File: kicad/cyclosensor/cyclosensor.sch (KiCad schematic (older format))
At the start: 5 parts, among them J1 RJ14, J2 RJ14, U1 TCRT5000, U2 TCRT5000

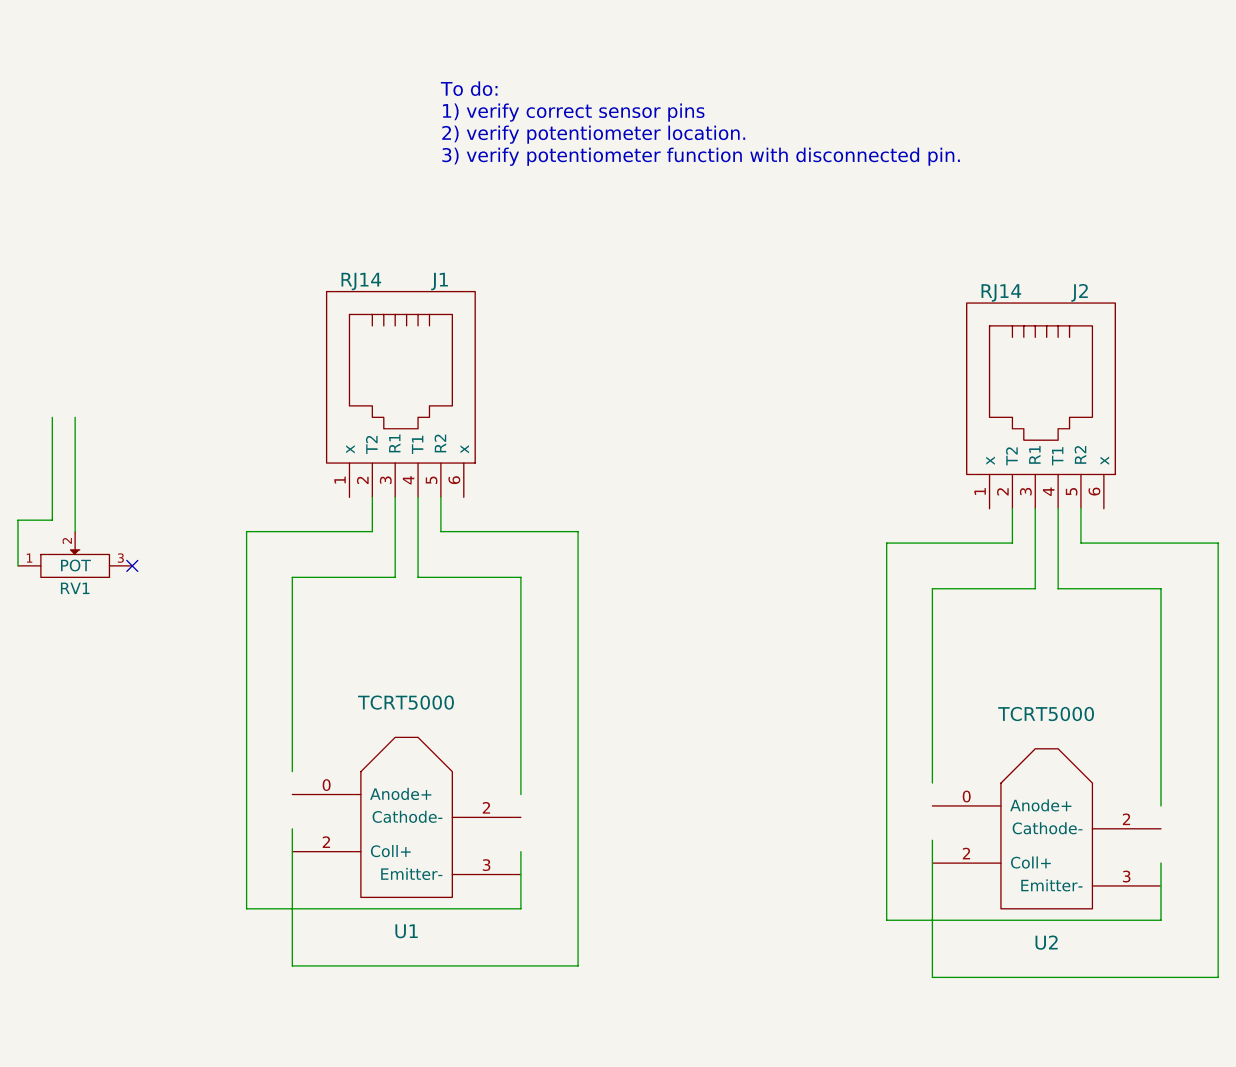
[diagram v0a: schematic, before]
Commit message: updating basic cyclo-sensor.  Still need to verify with actual cyclophone.
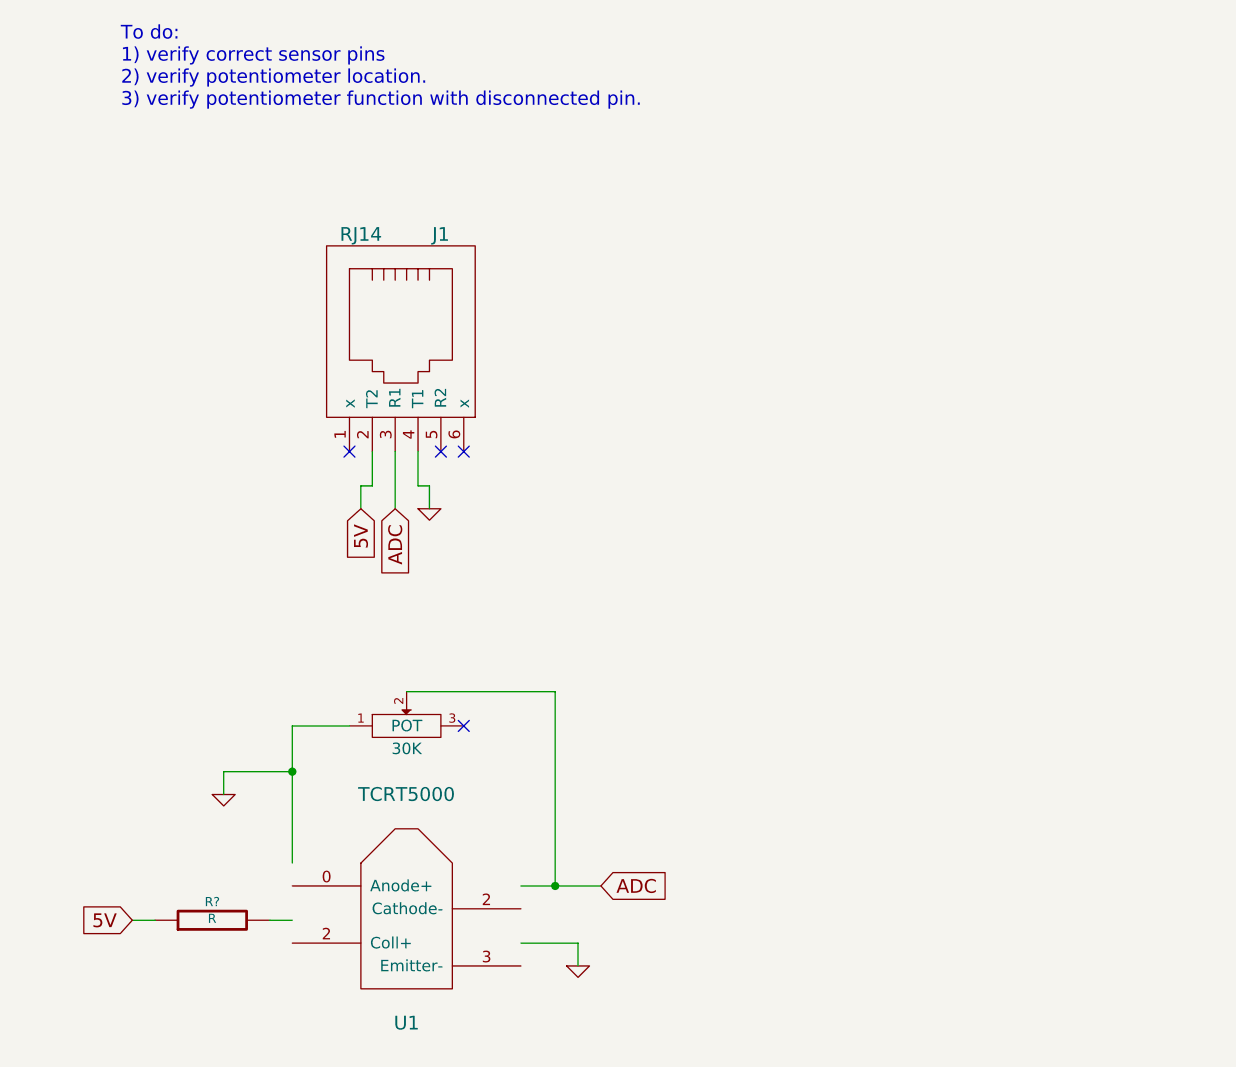
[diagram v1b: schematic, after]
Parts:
- removed J2: RJ14, ~, symbol RJ14
- removed RV1: POT, symbol POT
- removed U2: TCRT5000, symbol TCRT5000
- added 30K: POT, ~, symbol POT
- added R?: R, ~, symbol R
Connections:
- net labels added: 5V, ADC, GND
- wire segments 36 -> 20
- no-connect marks 1 -> 4
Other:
- moved on the sheet: J1, U1
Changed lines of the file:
@@
 Sheet 1 1
 Title ""
-Date "2 apr 2014"
+Date "6 apr 2014"
 Rev ""
 Comp ""
@@
 L RJ14 J1
 U 1 1 532FB492
-P 4800 3150
-F 0 "J1" H 5000 3650 60  0000 C CNN
-F 1 "RJ14" H 4650 3650 60  0000 C CNN
-F 2 "~" H 4800 3150 60  0000 C CNN
-F 3 "~" H 4800 3150 60  0000 C CNN
-	1    4800 3150
+P 4800 2950
+F 0 "J1" H 5000 3450 60  0000 C CNN
+F 1 "RJ14" H 4650 3450 60  0000 C CNN
+F 2 "~" H 4800 2950 60  0000 C CNN
+F 3 "~" H 4800 2950 60  0000 C CNN
+	1    4800 2950
 	1    0    0    -1
 $EndComp
@@
 L TCRT5000 U1
 U 1 1 532FB498
-P 4850 4950
-F 0 "U1" H 4850 4400 60  0000 C CNN
-F 1 "TCRT5000" H 4850 5400 60  0000 C CNN
-F 2 "" H 4850 4950 60  0000 C CNN
-F 3 "" H 4850 4950 60  0000 C CNN
-	1    4850 4950
+P 4850 5350
+F 0 "U1" H 4850 4800 60  0000 C CNN
+F 1 "TCRT5000" H 4850 5800 60  0000 C CNN
+F 2 "" H 4850 5350 60  0000 C CNN
+F 3 "" H 4850 5350 60  0000 C CNN
+	1    4850 5350
+	1    0    0    -1
+$EndComp
+Text Notes 3600 1900 0    60   ~ 0
+To do:\n1) verify correct sensor pins\n2) verify potentiometer location.\n3) verify potentiometer function with disconnected pin.
+Text GLabel 4650 3650 3    60   Input ~ 0
+5V
+Text GLabel 4800 3650 3    60   Input ~ 0
+ADC
+$Comp
+L GND #PWR?
+U 1 1 534162D0
+P 4950 3650
+F 0 "#PWR?" H 4950 3650 30  0001 C CNN
+F 1 "GND" H 4950 3580 30  0001 C CNN
+F 2 "" H 4950 3650 60  0000 C CNN
+F 3 "" H 4950 3650 60  0000 C CNN
+	1    4950 3650
+	1    0    0    -1
+$EndComp
+Text GLabel 3650 5450 0    60   Input ~ 0
+5V
+Text GLabel 5700 5300 2    60   Input ~ 0
+ADC
+$Comp
+L GND #PWR?
+U 1 1 534163B6
+P 5600 5650
+F 0 "#PWR?" H 5600 5650 30  0001 C CNN
+F 1 "GND" H 5600 5580 30  0001 C CNN
+F 2 "" H 5600 5650 60  0000 C CNN
+F 3 "" H 5600 5650 60  0000 C CNN
+	1    5600 5650
+	1    0    0    -1
+$EndComp
+$Comp
+L R R?
+U 1 1 534163EA
+P 4000 5450
+F 0 "R?" V 4080 5450 40  0000 C CNN
+F 1 "R" V 4007 5451 40  0000 C CNN
+F 2 "~" V 3930 5450 30  0000 C CNN
+F 3 "~" H 4000 5450 30  0000 C CNN
+	1    4000 5450
+	0    -1   -1   0
+$EndComp
+Wire Wire Line
+	4700 3400 4700 3550
+Wire Wire Line
+	4700 3550 4650 3550
+Wire Wire Line
+	4650 3550 4650 3650
+Wire Wire Line
+	4800 3400 4800 3650
+Wire Wire Line
+	4900 3400 4900 3550
+Wire Wire Line
+	4900 3550 4950 3550
+Wire Wire Line
+	4950 3550 4950 3650
+Wire Wire Line
+	5350 5550 5600 5550
+Wire Wire Line
+	5600 5550 5600 5650
+Wire Wire Line
+	4250 5450 4350 5450
+Wire Wire Line
+	3650 5450 3750 5450
+$Comp
+L POT 30K
+U 1 1 5341646B
+P 4850 4600
+F 0 "30K" H 4850 4500 50  0000 C CNN
+F 1 "POT" H 4850 4600 50  0000 C CNN
+F 2 "~" H 4850 4600 60  0000 C CNN
+F 3 "~" H 4850 4600 60  0000 C CNN
+	1    4850 4600
+	1    0    0    -1
+$EndComp
+$Comp
+L GND #PWR?
+U 1 1 53416487
+P 4050 4900
+F 0 "#PWR?" H 4050 4900 30  0001 C CNN
+F 1 "GND" H 4050 4830 30  0001 C CNN
+F 2 "" H 4050 4900 60  0000 C CNN
+F 3 "" H 4050 4900 60  0000 C CNN
+	1    4050 4900
 	1    0    0    -1
 $EndComp
 Wire Wire Line
-	5350 5150 5350 5400
+	4350 4600 4350 4800
 Wire Wire Line
-	5350 5400 4150 5400
+	4350 4800 4350 5200
 Wire Wire Line
-	4150 5400 4150 3750
+	4350 4600 4600 4600
+Connection ~ 4350 4800
 Wire Wire Line
-	4150 3750 4700 3750
+	4850 4450 5500 4450
 Wire Wire Line
-	4700 3750 4700 3600
+	5500 4450 5500 5300
 Wire Wire Line
-	4350 4800 4350 3950
+	5350 5300 5500 5300
 Wire Wire Line
-	3300 3250 3300 3700
+	5500 5300 5700 5300
+Connection ~ 5500 5300
 Wire Wire Line
-	3400 3250 3400 3750
+	4050 4900 4050 4800
 Wire Wire Line
-	5350 3950 5350 4900
-Wire Wire Line
-	4350 5050 4350 5650
-Wire Wire Line
-	4350 5650 5600 5650
-Wire Wire Line
-	5600 5650 5600 3750
-Wire Wire Line
-	5600 3750 5000 3750
-Wire Wire Line
-	5000 3750 5000 3600
-Text Notes 5000 2150 0    60   ~ 0
-To do:\n1) verify correct sensor pins\n2) verify potentiometer location.\n3) verify potentiometer function with disconnected pin.
-$Comp
-L POT RV1
-U 1 1 5330B579
-P 3400 3900
-F 0 "RV1" H 3400 3800 50  0000 C CNN
-F 1 "POT" H 3400 3900 50  0000 C CNN
-F 2 "" H 3400 3900 60  0000 C CNN
-F 3 "" H 3400 3900 60  0000 C CNN
-	1    3400 3900
-	1    0    0    -1
-$EndComp
-NoConn ~ 3650 3900
-Wire Wire Line
-	3300 3700 3150 3700
-Wire Wire Line
-	3150 3700 3150 3900
-$Comp
-L RJ14 J2
-U 1 1 5338F808
-P 7600 3200
-F 0 "J2" H 7800 3700 60  0000 C CNN
-F 1 "RJ14" H 7450 3700 60  0000 C CNN
-F 2 "~" H 7600 3200 60  0000 C CNN
-F 3 "~" H 7600 3200 60  0000 C CNN
-	1    7600 3200
-	1    0    0    -1
-$EndComp
-$Comp
-L TCRT5000 U2
-U 1 1 5338F80E
-P 7650 5000
-F 0 "U2" H 7650 4450 60  0000 C CNN
-F 1 "TCRT5000" H 7650 5450 60  0000 C CNN
-F 2 "" H 7650 5000 60  0000 C CNN
-F 3 "" H 7650 5000 60  0000 C CNN
-	1    7650 5000
-	1    0    0    -1
-$EndComp
-Wire Wire Line
-	8150 5200 8150 5450
-Wire Wire Line
-	8150 5450 6950 5450
-Wire Wire Line
-	6950 5450 6950 3800
-Wire Wire Line
-	6950 3800 7500 3800
-Wire Wire Line
-	7500 3800 7500 3650
-Wire Wire Line
-	7150 4850 7150 4000
-Wire Wire Line
-	8150 4000 8150 4950
-Wire Wire Line
-	7150 5100 7150 5700
-Wire Wire Line
-	7150 5700 8400 5700
-Wire Wire Line
-	8400 5700 8400 3800
-Wire Wire Line
-	8400 3800 7800 3800
-Wire Wire Line
-	7800 3800 7800 3650
-Wire Wire Line
-	4800 3600 4800 3950
-Wire Wire Line
-	4800 3950 4350 3950
-Wire Wire Line
-	4900 3600 4900 3950
-Wire Wire Line
-	4900 3950 5350 3950
-Wire Wire Line
-	7700 3650 7700 4000
-Wire Wire Line
-	7700 4000 8150 4000
-Wire Wire Line
-	7150 4000 7600 4000
-Wire Wire Line
-	7600 4000 7600 3650
+	4050 4800 4350 4800
+NoConn ~ 5100 4600
+NoConn ~ 4600 3400
+NoConn ~ 5000 3400
+NoConn ~ 5100 3400
 $EndSCHEMATC

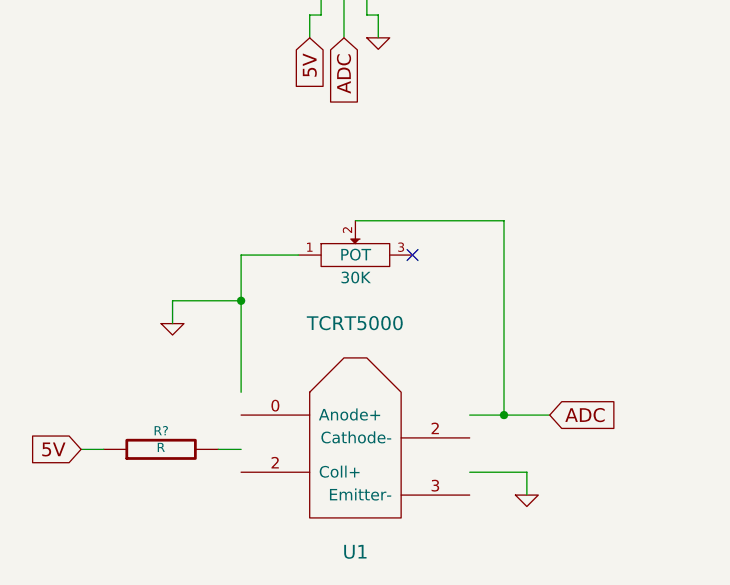
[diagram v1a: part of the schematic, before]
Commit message: add two voltage regulation circuits, the TL431 and LM317 based.  Also update some things - REFP is 2.5v, while AREF is 5v
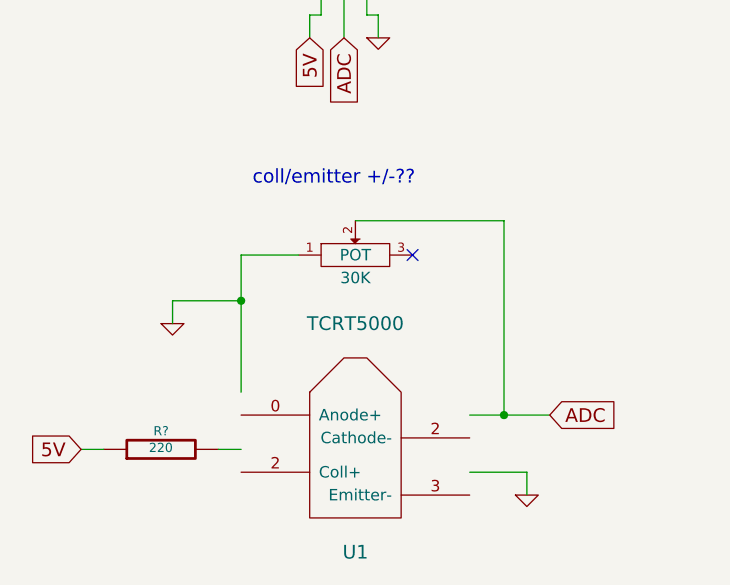
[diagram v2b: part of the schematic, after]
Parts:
- R?: value R -> 220
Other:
- note added: "coll/emitter +/-??"
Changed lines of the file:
@@
 P 4000 5450
 F 0 "R?" V 4080 5450 40  0000 C CNN
-F 1 "R" V 4007 5451 40  0000 C CNN
+F 1 "220" V 4007 5451 40  0000 C CNN
 F 2 "~" V 3930 5450 30  0000 C CNN
 F 3 "~" H 4000 5450 30  0000 C CNN
@@
 NoConn ~ 5000 3400
 NoConn ~ 5100 3400
+Text Notes 4400 4300 0    60   ~ 0
+coll/emitter +/-??
 $EndSCHEMATC

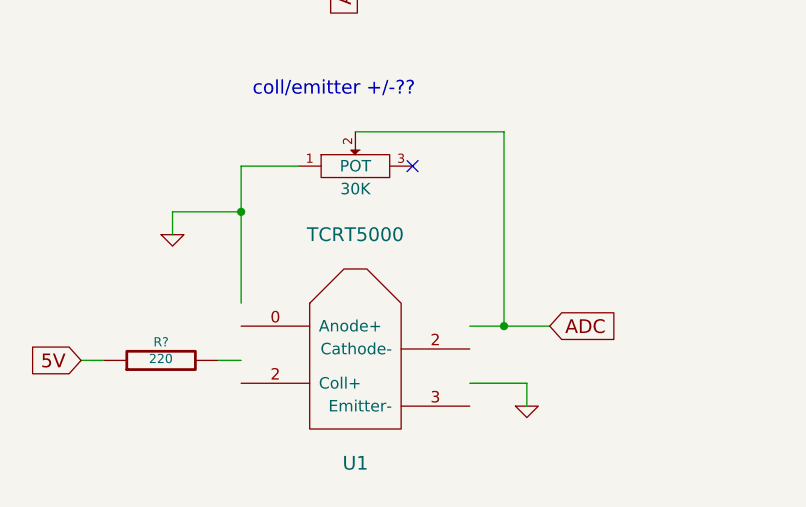
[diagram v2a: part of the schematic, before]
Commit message: remove PI pins, power regulator thingy, add optional DIO connector.
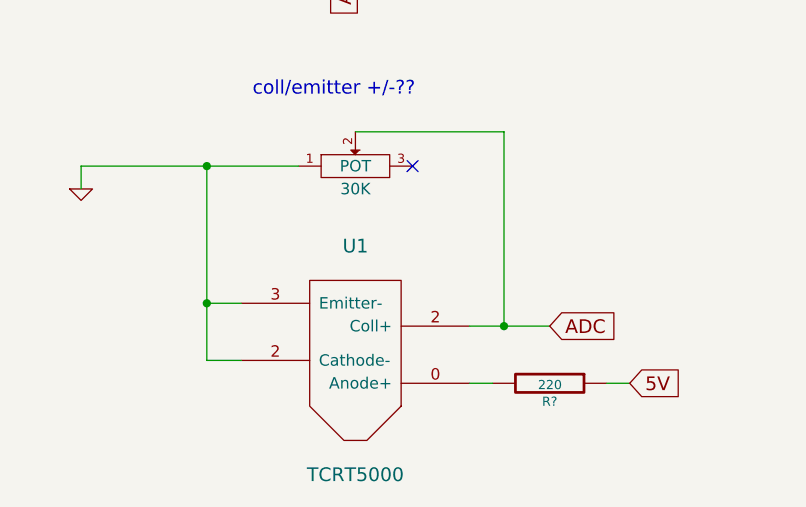
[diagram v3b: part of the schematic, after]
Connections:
- wire segments 20 -> 17
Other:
- moved on the sheet: R?, U1
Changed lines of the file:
@@
 Sheet 1 1
 Title ""
-Date "6 apr 2014"
+Date "13 apr 2014"
 Rev ""
 Comp ""
@@
 L TCRT5000 U1
 U 1 1 532FB498
-P 4850 5350
-F 0 "U1" H 4850 4800 60  0000 C CNN
-F 1 "TCRT5000" H 4850 5800 60  0000 C CNN
-F 2 "" H 4850 5350 60  0000 C CNN
-F 3 "" H 4850 5350 60  0000 C CNN
-	1    4850 5350
-	1    0    0    -1
+P 4850 5500
+F 0 "U1" H 4850 4950 60  0000 C CNN
+F 1 "TCRT5000" H 4850 5950 60  0000 C CNN
+F 2 "" H 4850 5500 60  0000 C CNN
+F 3 "" H 4850 5500 60  0000 C CNN
+	1    4850 5500
+	-1   0    0    1
 $EndComp
 Text Notes 3600 1900 0    60   ~ 0
@@
 	1    0    0    -1
 $EndComp
-Text GLabel 3650 5450 0    60   Input ~ 0
+Text GLabel 6050 5550 2    60   Input ~ 0
 5V
 Text GLabel 5700 5300 2    60   Input ~ 0
 ADC
 $Comp
-L GND #PWR?
-U 1 1 534163B6
-P 5600 5650
-F 0 "#PWR?" H 5600 5650 30  0001 C CNN
-F 1 "GND" H 5600 5580 30  0001 C CNN
-F 2 "" H 5600 5650 60  0000 C CNN
-F 3 "" H 5600 5650 60  0000 C CNN
-	1    5600 5650
-	1    0    0    -1
-$EndComp
-$Comp
 L R R?
 U 1 1 534163EA
-P 4000 5450
-F 0 "R?" V 4080 5450 40  0000 C CNN
-F 1 "220" V 4007 5451 40  0000 C CNN
-F 2 "~" V 3930 5450 30  0000 C CNN
-F 3 "~" H 4000 5450 30  0000 C CNN
-	1    4000 5450
-	0    -1   -1   0
+P 5700 5550
+F 0 "R?" V 5780 5550 40  0000 C CNN
+F 1 "220" V 5707 5551 40  0000 C CNN
+F 2 "~" V 5630 5550 30  0000 C CNN
+F 3 "~" H 5700 5550 30  0000 C CNN
+	1    5700 5550
+	0    1    1    0
 $EndComp
 Wire Wire Line
@@
 	4950 3550 4950 3650
 Wire Wire Line
-	5350 5550 5600 5550
+	5450 5550 5350 5550
 Wire Wire Line
-	5600 5550 5600 5650
-Wire Wire Line
-	4250 5450 4350 5450
-Wire Wire Line
-	3650 5450 3750 5450
+	6050 5550 5950 5550
 $Comp
 L POT 30K
@@
 L GND #PWR?
 U 1 1 53416487
-P 4050 4900
-F 0 "#PWR?" H 4050 4900 30  0001 C CNN
-F 1 "GND" H 4050 4830 30  0001 C CNN
-F 2 "" H 4050 4900 60  0000 C CNN
-F 3 "" H 4050 4900 60  0000 C CNN
-	1    4050 4900
+P 3650 4700
+F 0 "#PWR?" H 3650 4700 30  0001 C CNN
+F 1 "GND" H 3650 4630 30  0001 C CNN
+F 2 "" H 3650 4700 60  0000 C CNN
+F 3 "" H 3650 4700 60  0000 C CNN
+	1    3650 4700
 	1    0    0    -1
 $EndComp
-Wire Wire Line
-	4350 4600 4350 4800
-Wire Wire Line
-	4350 4800 4350 5200
-Wire Wire Line
-	4350 4600 4600 4600
-Connection ~ 4350 4800
 Wire Wire Line
 	4850 4450 5500 4450
@@
 	5500 4450 5500 5300
 Wire Wire Line
-	5350 5300 5500 5300
-Wire Wire Line
-	5500 5300 5700 5300
+	5350 5300 5700 5300
 Connection ~ 5500 5300
 Wire Wire Line
-	4050 4900 4050 4800
+	3650 4700 3650 4600
 Wire Wire Line
-	4050 4800 4350 4800
+	3650 4600 4600 4600
 NoConn ~ 5100 4600
 NoConn ~ 4600 3400
@@
 Text Notes 4400 4300 0    60   ~ 0
 coll/emitter +/-??
+Wire Wire Line
+	4200 4600 4200 5450
+Wire Wire Line
+	4200 5200 4350 5200
+Connection ~ 4200 4600
+Wire Wire Line
+	4200 5450 4350 5450
+Connection ~ 4200 5200
 $EndSCHEMATC
